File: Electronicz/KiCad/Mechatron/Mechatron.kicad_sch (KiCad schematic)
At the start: 28 parts, among them J1 ESP 32 L, J10 Ultra 4, J11 Ultra 5, J12 Ultra 6, J13 Ultra 7, J14 Ultra 8, J15 Battery, J16 LED1 Out, J17 LED3 Out, J18 LED3 Out, J19 Servo 3, J2 ESP 32 R, J20 Servo 2, J21 Servo 1, J3 Motor 1, J4 Motor 2, J5 Motor 3, J6 Motor 4, J7 Ultra 1, J8 Ultra 2, J9 Ultra 3, Q1 Q_PNP_CBE, Q2 Q_PNP_CBE, Q3 Q_PNP_CBE, Q4 Q_PNP_CBE, Q5 Q_PNP_CBE, Q6 Q_PNP_CBE, Q7 Q_PNP_CBE

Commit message: update schematic and create PCB
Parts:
- added R1, R2, R3: R, Resistor_THT:R_Axial_DIN0207_L6.3mm_D2.5mm_P10.16mm_Horizontal, symbol Device:R
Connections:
- net at Q2.3 (E): now also J21.1 (Pin_1); no longer J21.2 (Pin_2)
- net at J3.2 (Pin_2): now also J1.2 (Pin_2), J10.4 (Pin_4), J11.4 (Pin_4), J12.4 (Pin_4), J13.4 (Pin_4), J14.4 (Pin_4), J15.1 (Pin_1), J16.2 (Pin_2), J17.2 (Pin_2), J18.2 (Pin_2), J19.2 (Pin_2), J2.2 (Pin_2), J20.2 (Pin_2), J21.2 (Pin_2), J4.2 (Pin_2), J5.2 (Pin_2), J6.2 (Pin_2), J7.4 (Pin_4), J8.4 (Pin_4), J9.4 (Pin_4), Q1.2 (B), Q2.2 (B), Q3.2 (B), Q4.2 (B); no longer J2.6 (Pin_6)
- net at J3.4 (Pin_4): now also J2.7 (Pin_7); no longer J2.10 (Pin_10)
- net at J2.9 (Pin_9): now also J4.4 (Pin_4); no longer J6.2 (Pin_2)
- net at Q3.3 (E): now also J20.1 (Pin_1); no longer J20.2 (Pin_2)
- net at J1.6 (Pin_6): now also J9.1 (Pin_1); no longer J9.2 (Pin_2)
- net at J10.3 (Pin_3), J11.3 (Pin_3), J12.3 (Pin_3)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: now also Q1.3 (E), Q5.1 (C), Q6.1 (C), Q7.1 (C); no longer J1.3 (Pin_3)
- net at Q5.2 (B): now also R3.2; no longer J1.12 (Pin_12)
- net at J14.2 (Pin_2): now also J1.3 (Pin_3), J10.2 (Pin_2), J11.2 (Pin_2), J12.2 (Pin_2), J13.2 (Pin_2), J7.2 (Pin_2), J8.2 (Pin_2), J9.2 (Pin_2); no longer J1.11 (Pin_11)
- net at J1.9 (Pin_9): now also J12.1 (Pin_1); no longer J12.2 (Pin_2)
- net at J1.8 (Pin_8): now also J11.1 (Pin_1); no longer J11.2 (Pin_2)
- net at J1.5 (Pin_5): now also J8.1 (Pin_1); no longer J8.2 (Pin_2)
- net at J2.8 (Pin_8): now also J4.3 (Pin_3); no longer J5.2 (Pin_2)
- net at J2.12 (Pin_12): now also J6.3 (Pin_3); no longer J5.4 (Pin_4)
- net at Q4.3 (E): now also J19.1 (Pin_1); no longer J19.2 (Pin_2)
- net at J2.11 (Pin_11): now also J5.4 (Pin_4); no longer J4.4 (Pin_4)
- net at J1.7 (Pin_7): now also J10.1 (Pin_1); no longer J10.2 (Pin_2)
- net at J1.10 (Pin_10): now also J13.1 (Pin_1); no longer J13.2 (Pin_2)
- net at J1.13 (Pin_13): now also R2.1; no longer Q6.2 (B)
- net at J1.14 (Pin_14): now also R1.1; no longer Q7.2 (B)
- net at J1.4 (Pin_4): now also J7.1 (Pin_1); no longer J7.2 (Pin_2)
- new net: J2.6 (Pin_6), J3.3 (Pin_3)
- new net: Q7.2 (B), R1.2
- new net: Q6.2 (B), R2.2
- new net: J1.11 (Pin_11), J14.1 (Pin_1)
- new net: J2.10 (Pin_10), J5.3 (Pin_3)
- new net: J1.12 (Pin_12), R3.1
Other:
- note added: "+ - Rotation PWM"
- note added: "Echo Trigger GND Vcc"
- note added: "PWM - +"
- note removed: "+ Rotation - PWM"
- note removed: "Ground Ecco Trigger Vcc"
- note removed: "PWM + -"

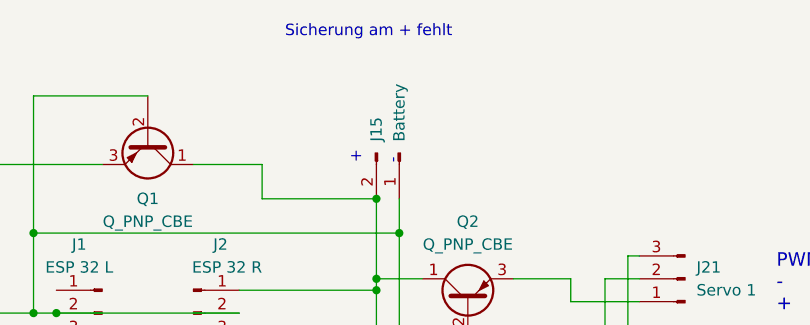
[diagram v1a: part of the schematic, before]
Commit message: change placement on the pcb
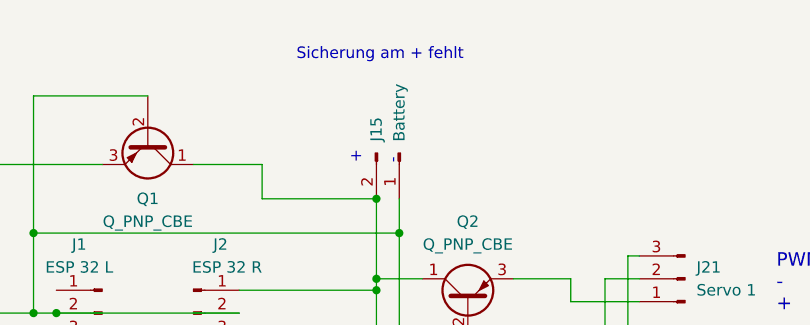
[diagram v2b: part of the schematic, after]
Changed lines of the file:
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@@
     (effects (font (size 1.5 1.5)) (justify left bottom))
   )
-  (text "Sicherung am + fehlt" (at 93.98 7.62 0)
+  (text "Sicherung am + fehlt" (at 95.25 10.16 0)
     (effects (font (size 1.27 1.27)) (justify left bottom))
   )

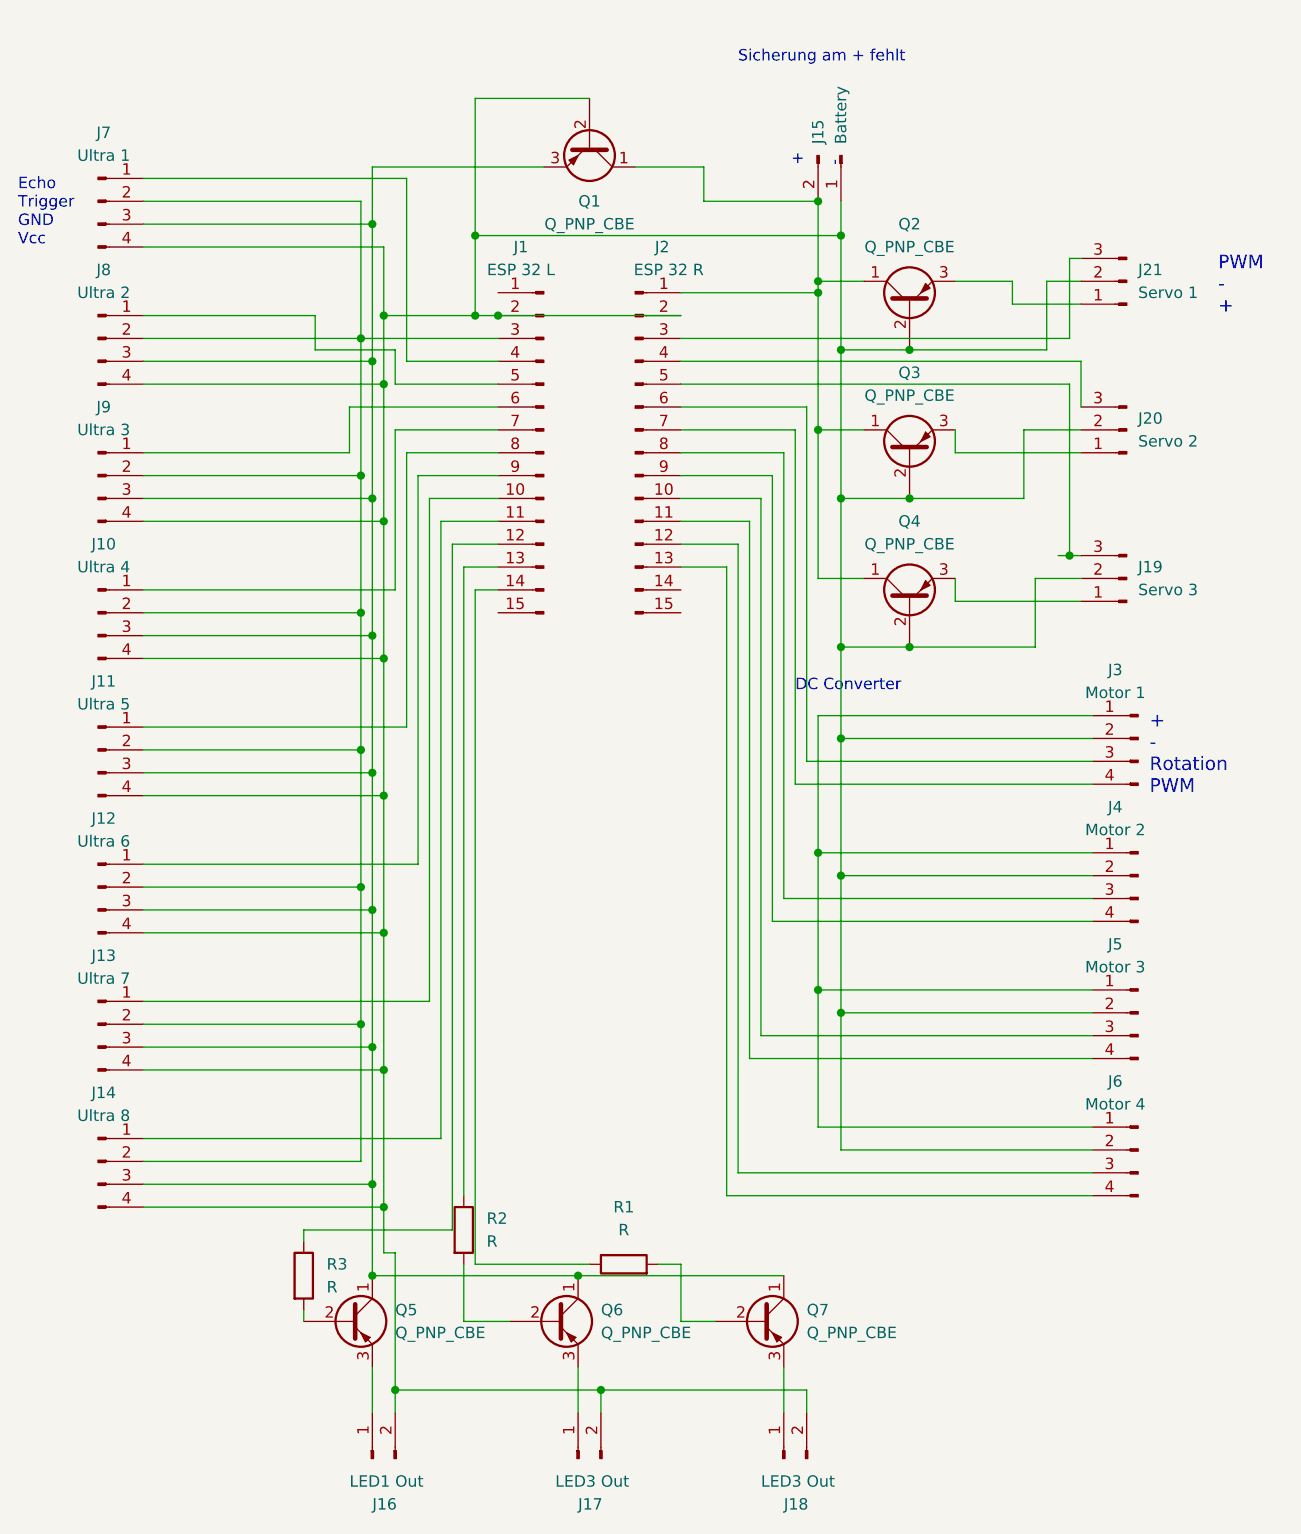
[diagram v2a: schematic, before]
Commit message: update schematic
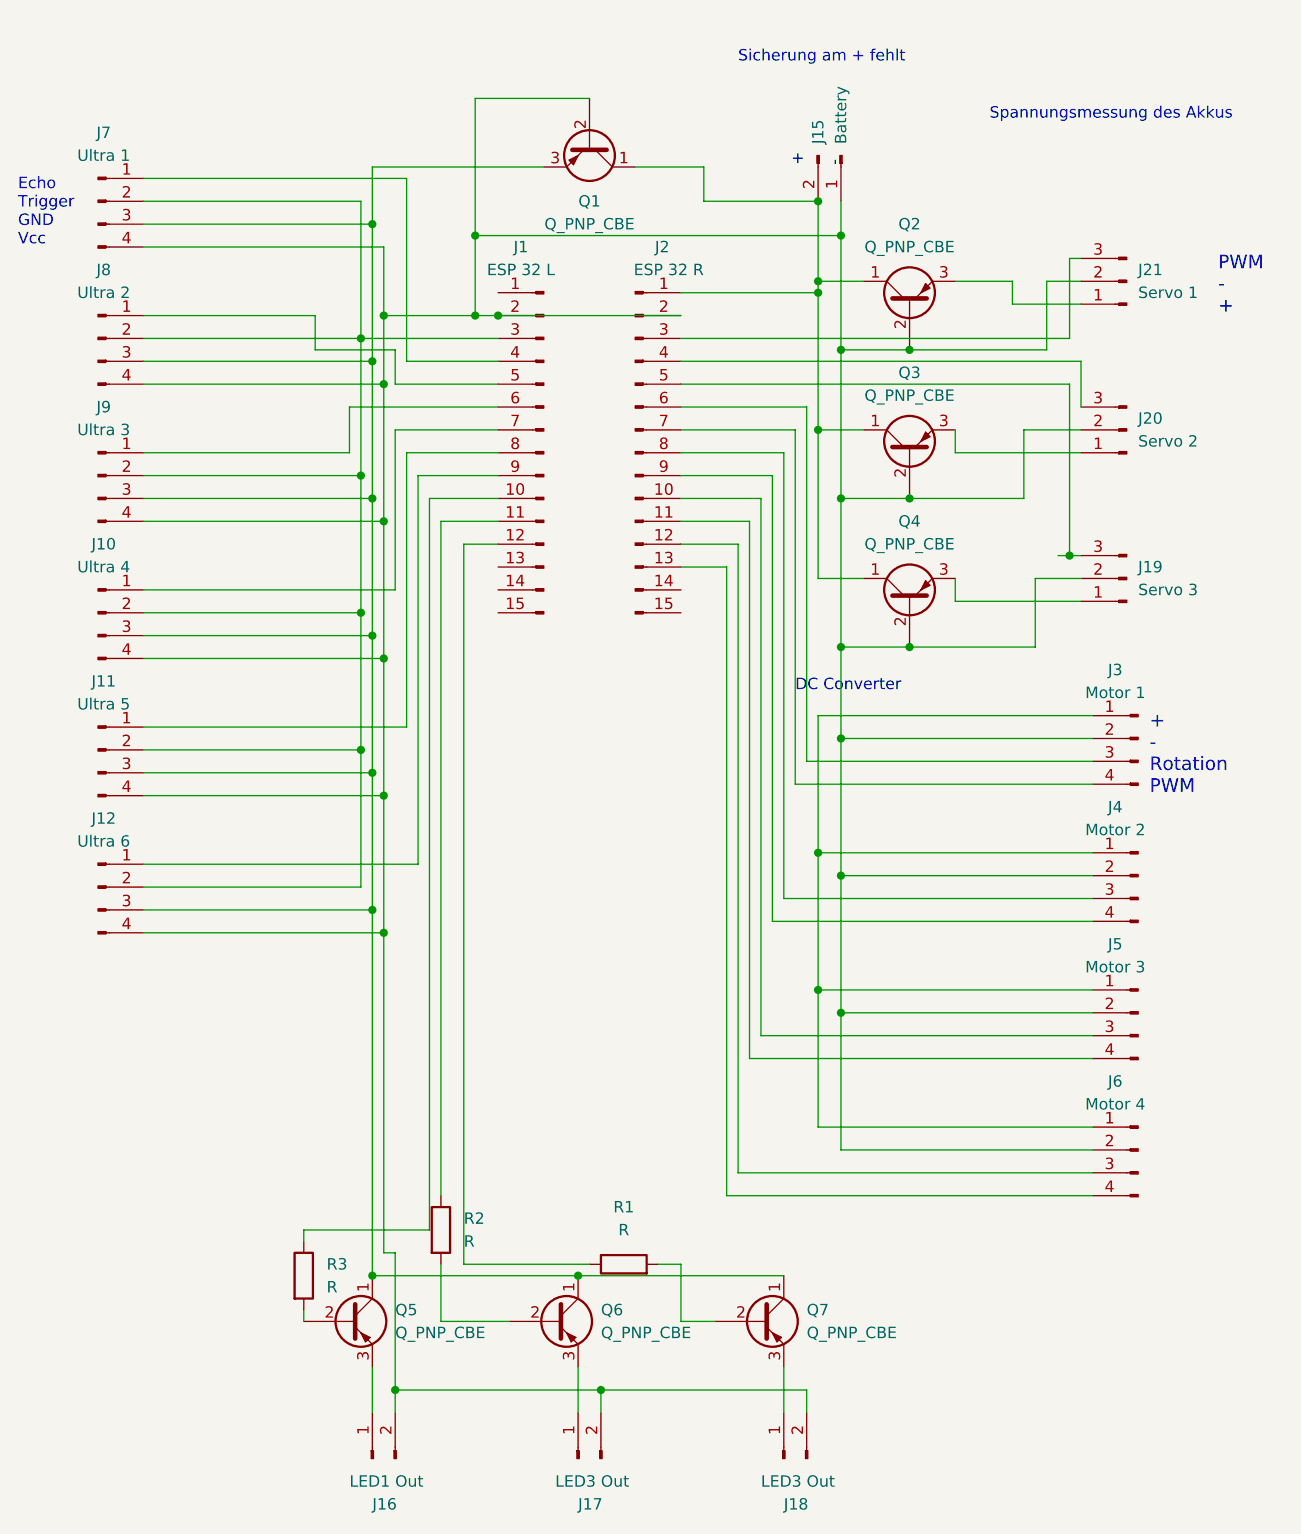
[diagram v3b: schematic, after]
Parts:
- removed J13: Ultra 7, Connector_PinHeader_2.54mm:PinHeader_1x04_P2.54mm_Vertical, symbol Connector:Conn_01x04_Pin
- removed J14: Ultra 8, Connector_PinHeader_2.54mm:PinHeader_1x04_P2.54mm_Vertical, symbol Connector:Conn_01x04_Pin
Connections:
- net at R1.1: now also J1.12 (Pin_12); no longer J1.14 (Pin_14)
- net at R2.1: now also J1.11 (Pin_11); no longer J1.13 (Pin_13)
- net at R3.1: now also J1.10 (Pin_10); no longer J1.12 (Pin_12)
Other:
- note added: "Spannungsmessung des Akkus"
- moved on the sheet: R2

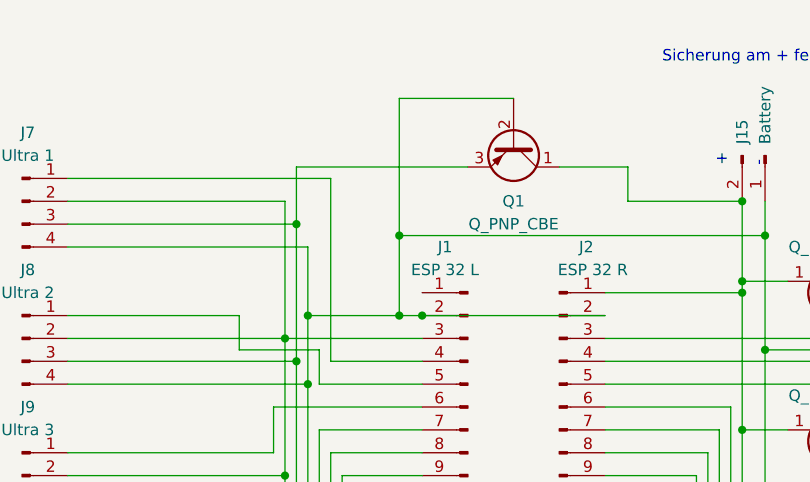
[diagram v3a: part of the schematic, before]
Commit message: update old schematic
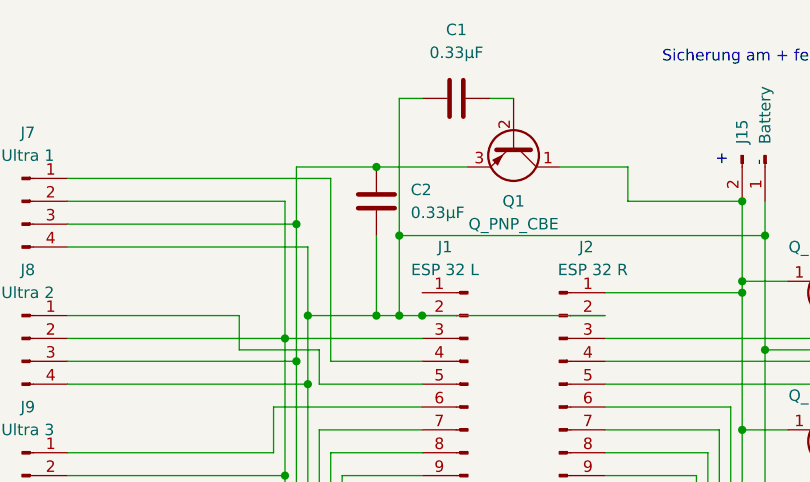
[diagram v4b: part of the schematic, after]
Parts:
- added C1, C2: 0.33µF, symbol Device:C
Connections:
- net at J1.2 (Pin_2), J10.4 (Pin_4), J11.4 (Pin_4)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: now also C1.1, C2.1; no longer Q1.2 (B)
- net at J10.3 (Pin_3), J11.3 (Pin_3), J12.3 (Pin_3)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: now also C2.2
- new net: C1.2, Q1.2 (B)
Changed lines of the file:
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@@
   (junction (at 54.61 27.94) (diameter 0) (color 0 0 0 0)
   )
+  (junction (at 63.5 38.1) (diameter 0) (color 0 0 0 0)
+  )
   (junction (at 54.61 73.66) (diameter 0) (color 0 0 0 0)
   )
@@
   (junction (at 55.88 38.1) (diameter 0) (color 0 0 0 0)
   )
+  (junction (at 63.5 21.59) (diameter 0) (color 0 0 0 0)
+  )
   (junction (at 55.88 91.44) (diameter 0) (color 0 0 0 0)
   )
@@
     (stroke (width 0) (type default))
   )
+  (wire (pts (xy 63.5 21.59) (xy 54.61 21.59))
+    (stroke (width 0) (type default))
+  )
   (wire (pts (xy 57.15 157.48) (xy 57.15 160.02))
     (stroke (width 0) (type default))
@@
     (stroke (width 0) (type default))
   )
-  (wire (pts (xy 78.74 13.97) (xy 66.04 13.97))
-    (stroke (width 0) (type default))
-  )
   (wire (pts (xy 68.58 50.8) (xy 57.15 50.8))
     (stroke (width 0) (type default))
@@
     (stroke (width 0) (type default))
   )
+  (wire (pts (xy 66.04 13.97) (xy 68.58 13.97))
+    (stroke (width 0) (type default))
+  )
   (wire (pts (xy 97.79 118.11) (xy 97.79 58.42))
     (stroke (width 0) (type default))
@@
     (stroke (width 0) (type default))
   )
+  (wire (pts (xy 63.5 38.1) (xy 66.04 38.1))
+    (stroke (width 0) (type default))
+  )
   (wire (pts (xy 57.15 157.48) (xy 80.01 157.48))
     (stroke (width 0) (type default))
@@
     (stroke (width 0) (type default))
   )
-  (wire (pts (xy 55.88 38.1) (xy 66.04 38.1))
-    (stroke (width 0) (type default))
-  )
-  (wire (pts (xy 73.66 21.59) (xy 54.61 21.59))
+  (wire (pts (xy 55.88 38.1) (xy 63.5 38.1))
+    (stroke (width 0) (type default))
+  )
+  (wire (pts (xy 73.66 21.59) (xy 63.5 21.59))
     (stroke (width 0) (type default))
   )
@@
     (stroke (width 0) (type default))
   )
+  (wire (pts (xy 76.2 13.97) (xy 78.74 13.97))
+    (stroke (width 0) (type default))
+  )
   (wire (pts (xy 114.3 41.91) (xy 129.54 41.91))
     (stroke (width 0) (type default))
@@
   )
   (wire (pts (xy 134.62 90.17) (xy 101.6 90.17))
+    (stroke (width 0) (type default))
+  )
+  (wire (pts (xy 63.5 29.21) (xy 63.5 38.1))
     (stroke (width 0) (type default))
   )
@@
         (path "/01788c3f-e6ba-44c1-b394-fb7624d63a9d"
           (reference "R2") (unit 1)
+        )
+      )
+    )
+  )
+  (symbol (lib_id "Device:C") (at 72.39 13.97 90) (unit 1)
+    (in_bom yes) (on_board yes) (dnp no) (fields_autoplaced)
+    (property "Reference" "C1" (at 72.39 6.35 90)
+      (effects (font (size 1.27 1.27)))
+    )
+    (property "Value" "0.33µF" (at 72.39 8.89 90)
+      (effects (font (size 1.27 1.27)))
+    )
+    (property "Footprint" "" (at 76.2 13.0048 0)
+      (effects (font (size 1.27 1.27)) hide)
+    )
+    (property "Datasheet" "~" (at 72.39 13.97 0)
+      (effects (font (size 1.27 1.27)) hide)
+    )
+    (pin "1")
+    (pin "2")
+    (instances
+      (project "Mechatron"
+        (path "/01788c3f-e6ba-44c1-b394-fb7624d63a9d"
+          (reference "C1") (unit 1)
         )
       )
@@
         )
       )
+    )
+  )
+  (symbol (lib_id "Device:C") (at 63.5 25.4 180) (unit 1)
+    (in_bom yes) (on_board yes) (dnp no) (fields_autoplaced)
+    (property "Reference" "C2" (at 67.31 24.13 0)
+      (effects (font (size 1.27 1.27)) (justify right))
+    )
+    (property "Value" "0.33µF" (at 67.31 26.67 0)
+      (effects (font (size 1.27 1.27)) (justify right))
+    )
+    (property "Footprint" "" (at 62.5348 21.59 0)
+      (effects (font (size 1.27 1.27)) hide)
+    )
+    (property "Datasheet" "~" (at 63.5 25.4 0)
+      (effects (font (size 1.27 1.27)) hide)
+    )
+    (pin "1")
+    (pin "2")
+    (instances
+      (project "Mechatron"
+        (path "/01788c3f-e6ba-44c1-b394-fb7624d63a9d"
+          (reference "C2") (unit 1)
+        )
+      )
